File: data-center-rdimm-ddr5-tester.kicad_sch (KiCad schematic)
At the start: 2 parts

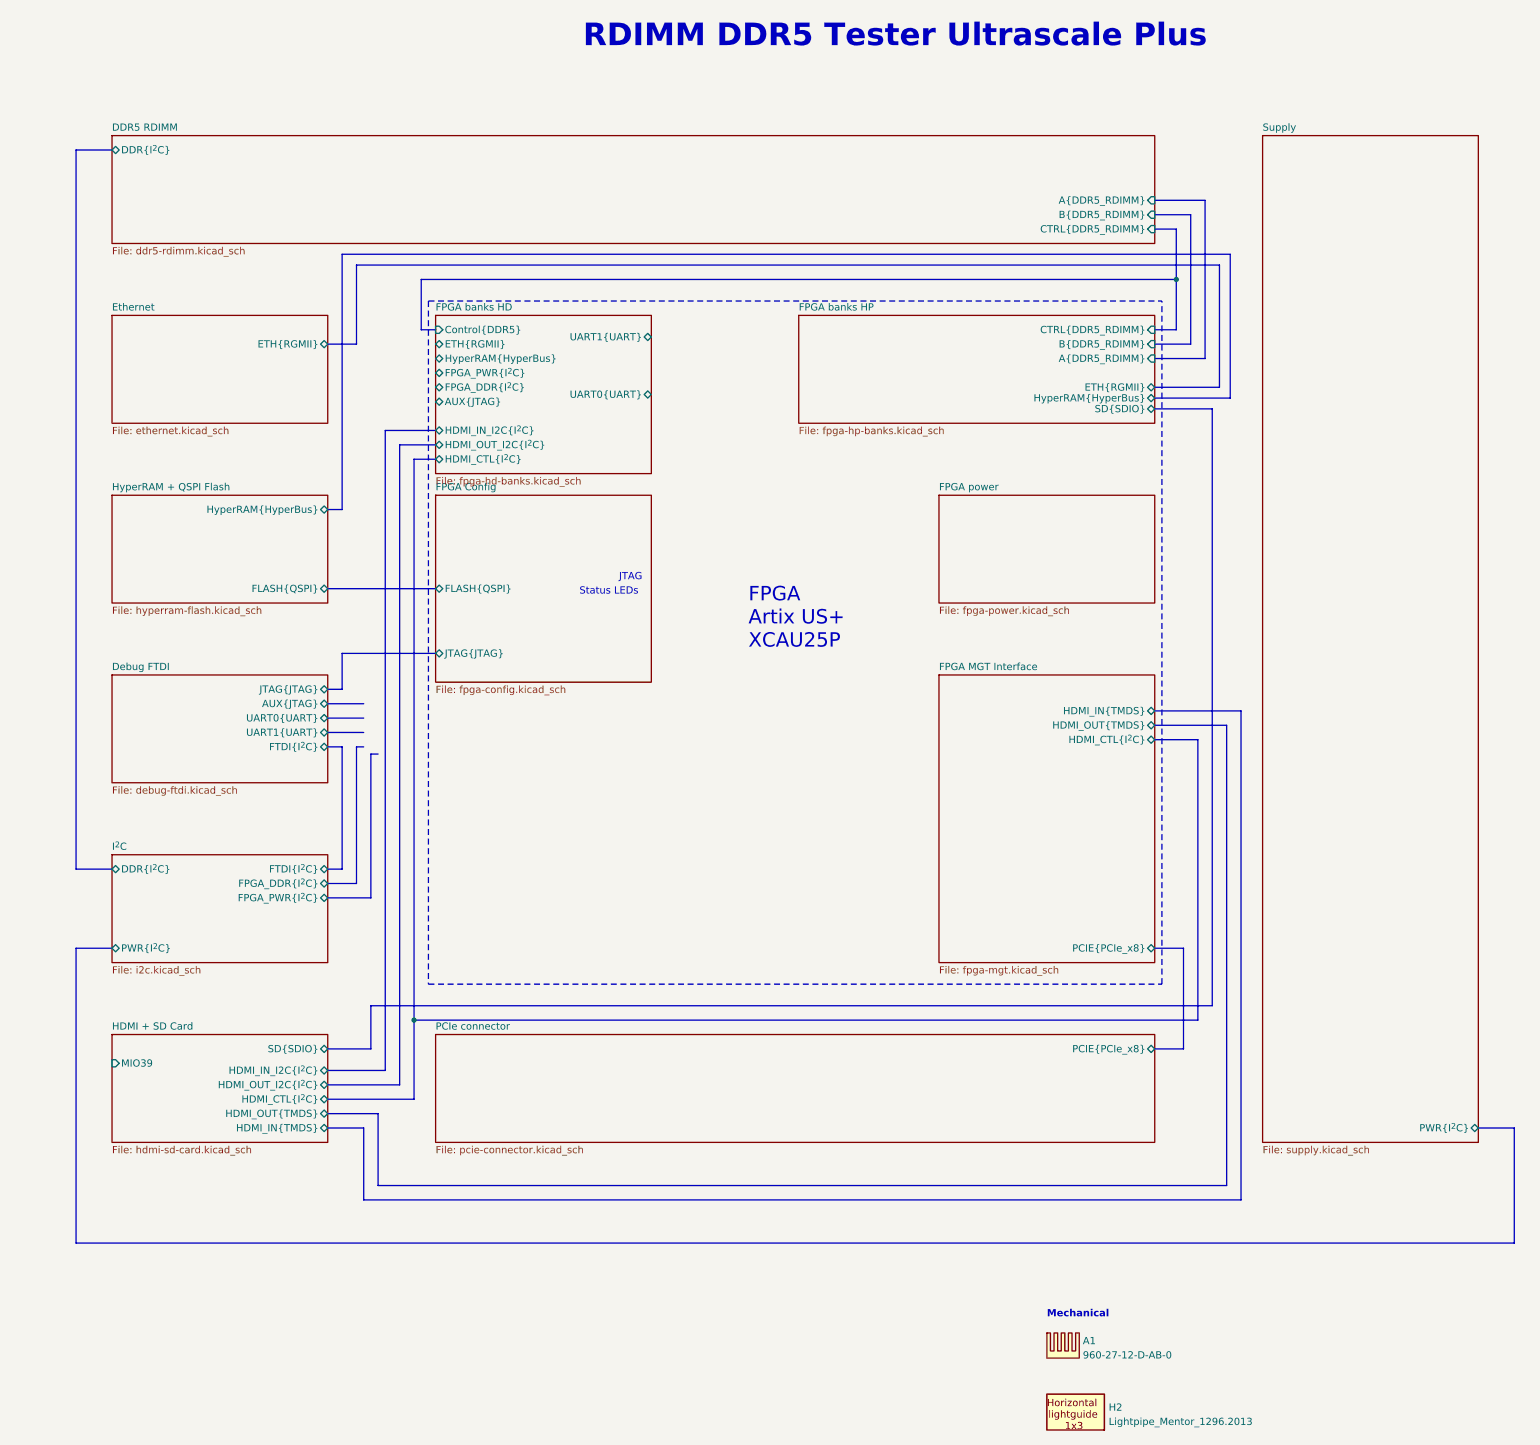
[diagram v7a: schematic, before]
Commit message: [#67402] Connect low speed signals and interfaces to the HD banks
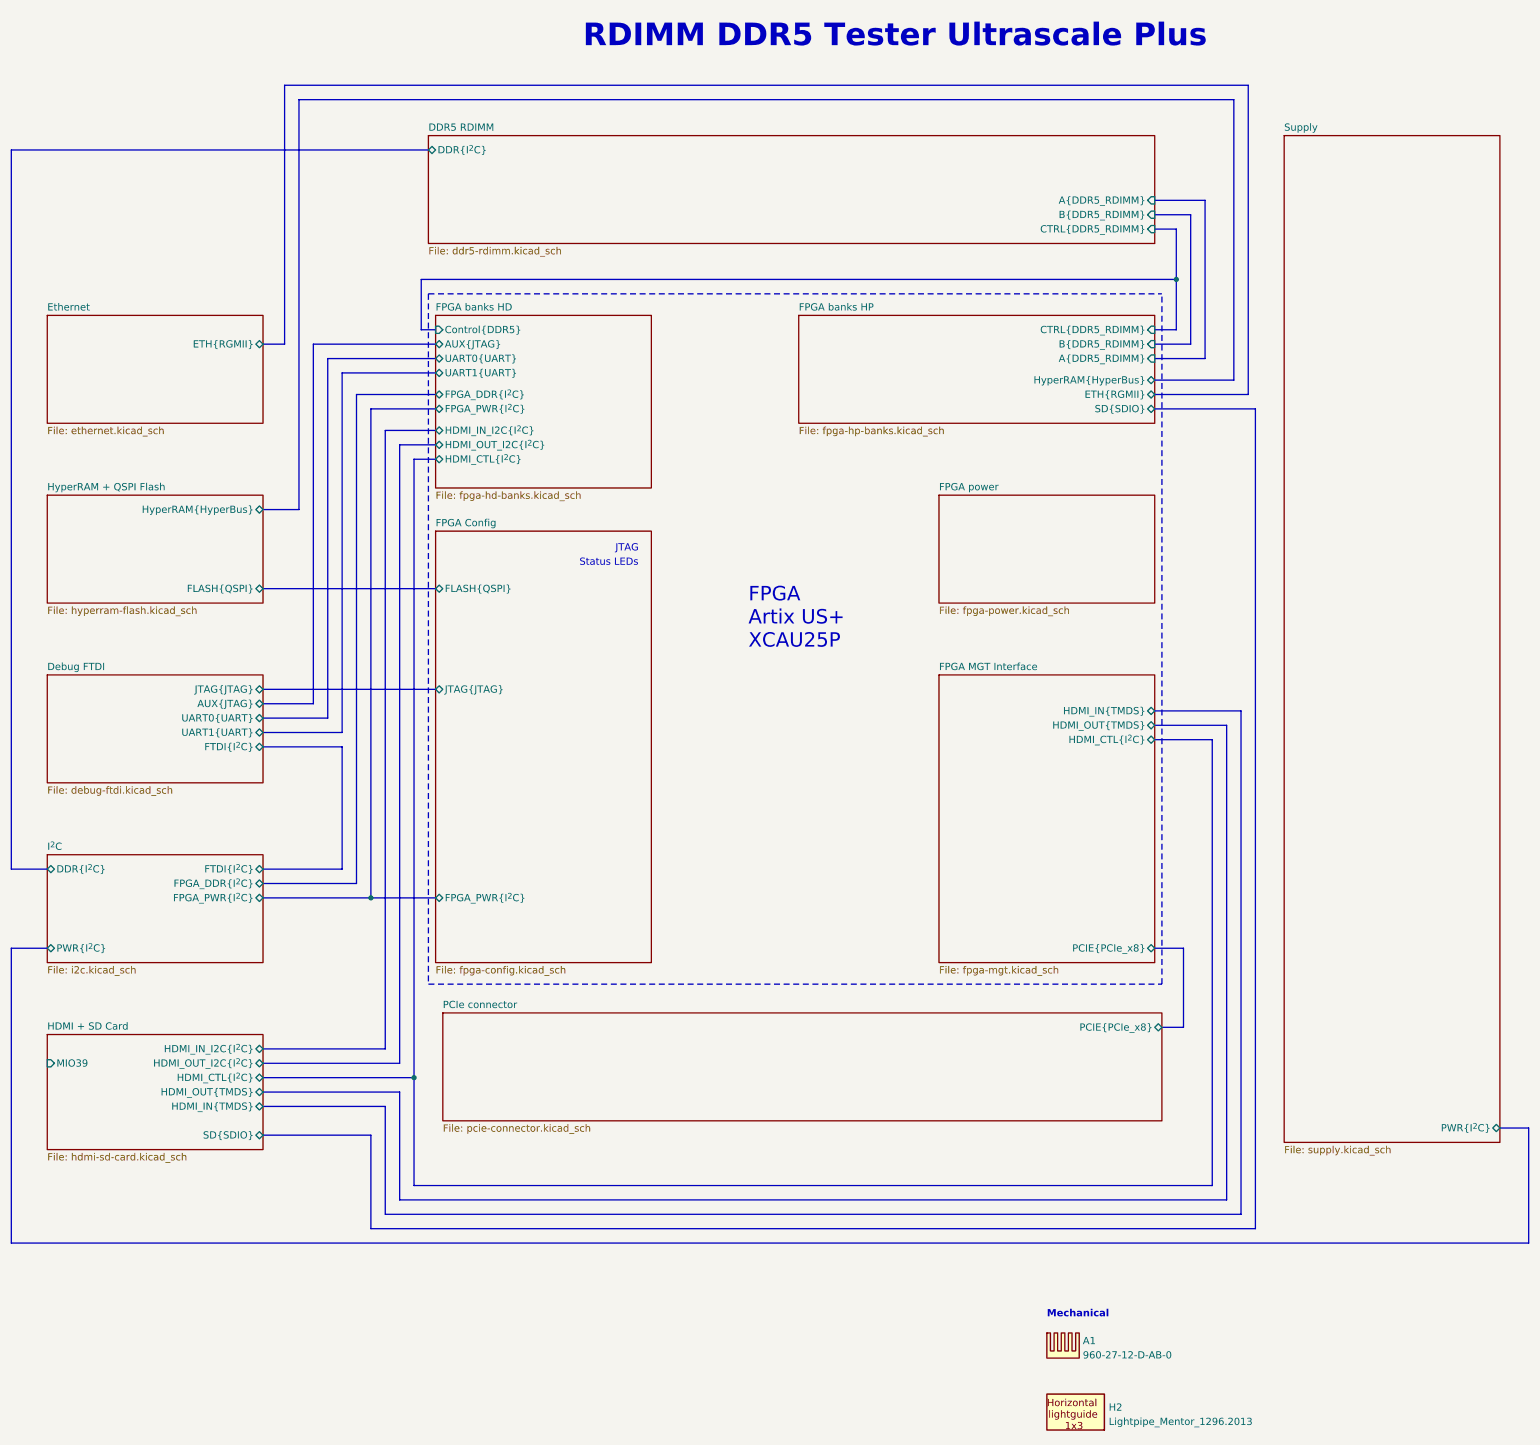
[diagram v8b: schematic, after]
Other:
- sheet FPGA Config ports: added FPGA_PWR{I^{2}C}; removed none
- sheet FPGA banks HD ports: added none; removed ETH{RGMII}, HyperRAM{HyperBus}
